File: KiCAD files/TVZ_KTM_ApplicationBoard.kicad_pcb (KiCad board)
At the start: 2 copper layers, 70 x 55 mm, 3 parts, among them J1 Conn_02x19_Odd_Even, J2 Conn_02x19_Odd_Even, U2 MCP2551-I-P

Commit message: update
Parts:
- added J3: Conn_02x19_Odd_Even, Connector_PinSocket_2.54mm:PinSocket_2x19_P2.54mm_Vertical_SMD, B.Cu at (180.5, 79.1)
- added J4: Conn_02x19_Odd_Even, Connector_PinSocket_2.54mm:PinSocket_2x19_P2.54mm_Vertical_SMD, B.Cu at (241.5, 79.1)
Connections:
- J1 pad 16: unconnected-(J1-Pad16) -> +3V3
- J1 pad 19: unconnected-(J1-Pad19) -> GND
- J1 pad 20: unconnected-(J1-Pad20) -> GND
- J1 pad 22: unconnected-(J1-Pad22) -> GND
- J1 pad 8: unconnected-(J1-Pad8) -> GND
- J2 pad 20: unconnected-(J2-Pad20) -> GND
- J2 pad 9: unconnected-(J2-Pad9) -> GND
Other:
- board size 70 x 55 mm -> 146 x 55 mm

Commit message: update
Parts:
- added C1: 100n X7R, Capacitor_SMD:C_0603_1608Metric, F.Cu at (116.4, 101.5)
- added C2: 100n X7R, Capacitor_SMD:C_0603_1608Metric, F.Cu at (215.0, 93.5)
- added C3: 100n X7R, Capacitor_SMD:C_0603_1608Metric, F.Cu at (219.0, 91.0)
- added C4: 100n X7R, Capacitor_SMD:C_0603_1608Metric, F.Cu at (215.0, 91.0)
- added D1: BLUE, LED_THT:LED_D5.0mm, F.Cu at (199.0, 62.0)
- added D10: RED, LED_THT:LED_D5.0mm, F.Cu at (130.0, 70.0)
- added D11: RED, LED_THT:LED_D5.0mm, F.Cu at (137.0, 70.0)
- added D12: RED, LED_THT:LED_D5.0mm, F.Cu at (144.0, 70.0)
- added D2: BLUE, LED_THT:LED_D5.0mm, F.Cu at (206.0, 62.0)
- added D3: BLUE, LED_THT:LED_D5.0mm, F.Cu at (213.0, 62.0)
- added D4: BLUE, LED_THT:LED_D5.0mm, F.Cu at (220.0, 62.0)
- added D5: GREEN, LED_THT:LED_D5.0mm, F.Cu at (123.0, 62.0)
- added D6: GREEN, LED_THT:LED_D5.0mm, F.Cu at (130.0, 62.0)
- added D7: GREEN, LED_THT:LED_D5.0mm, F.Cu at (137.0, 62.0)
- added D8: GREEN, LED_THT:LED_D5.0mm, F.Cu at (144.0, 62.0)
- added D9: RED, LED_THT:LED_D5.0mm, F.Cu at (123.0, 70.0)
- added JP1: Jumper_3_Open, Connector_PinHeader_2.54mm:PinHeader_1x03_P2.54mm_Vertical, F.Cu at (116.6, 88.9)
- added JP2: Jumper_2_Open, Connector_PinHeader_2.54mm:PinHeader_1x02_P2.54mm_Vertical, F.Cu at (137.4, 77.8)
- added JP3: Jumper_2_Open, Connector_PinHeader_2.54mm:PinHeader_1x02_P2.54mm_Vertical, F.Cu at (129.7, 87.5)
- added JP4: Jumper_3_Open, Connector_PinHeader_2.54mm:PinHeader_1x03_P2.54mm_Vertical, F.Cu at (132.7, 77.8)
- added JP5: Jumper_3_Open, Connector_PinHeader_2.54mm:PinHeader_1x03_P2.54mm_Vertical, F.Cu at (128.1, 77.8)
- added R1: 4k7, Resistor_SMD:R_0603_1608Metric, F.Cu at (124.9, 94.3)
- added R10: 220, Resistor_SMD:R_0603_1608Metric, F.Cu at (141.7, 76.8)
- added R11: 220, Resistor_SMD:R_0603_1608Metric, F.Cu at (149.7, 76.8)
- added R12: 220, Resistor_SMD:R_0603_1608Metric, F.Cu at (138.0, 86.5)
- added R13: 220, Resistor_SMD:R_0603_1608Metric, F.Cu at (145.7, 76.8)
- added R14: 220, Resistor_SMD:R_0603_1608Metric, F.Cu at (134.0, 91.5)
- added R15: 220, Resistor_SMD:R_0603_1608Metric, F.Cu at (129.3, 93.7)
- added R16: 220, Resistor_SMD:R_0603_1608Metric, F.Cu at (134.0, 89.0)
- added R17: 220, Resistor_SMD:R_0603_1608Metric, F.Cu at (145.7, 81.8)
- added R18: 220, Resistor_SMD:R_0603_1608Metric, F.Cu at (133.3, 94.0)
- added R19: 220, Resistor_SMD:R_0603_1608Metric, F.Cu at (138.0, 89.0)
- added R2: 4k7, Resistor_SMD:R_0603_1608Metric, F.Cu at (145.7, 79.3)
- added R3: 10k, Resistor_SMD:R_0603_1608Metric, F.Cu at (141.7, 81.8)
- added R4: 10k, Resistor_SMD:R_0603_1608Metric, F.Cu at (120.9, 94.3)
- added R5: 10k, Resistor_SMD:R_0603_1608Metric, F.Cu at (149.7, 79.3)
- added R6: 220, Resistor_SMD:R_0603_1608Metric, F.Cu at (142.0, 84.3)
- added R7: 220, Resistor_SMD:R_0603_1608Metric, F.Cu at (141.7, 79.3)
- added R8: 220, Resistor_SMD:R_0603_1608Metric, F.Cu at (134.0, 86.5)
- added R9: 220, Resistor_SMD:R_0603_1608Metric, F.Cu at (137.1, 84.0)
- added RV1: 10k, Footprints:Potentiometer_Bourns_3386P_Vertical, F.Cu at (119.8, 83.6)
- added SW1: OS102011MS2QN1, Footprints:OS102011MS2QN1, F.Cu at (198.0, 75.0)
- added SW2: OS102011MS2QN1, Footprints:OS102011MS2QN1, F.Cu at (214.0, 75.0)
- added SW3: OS102011MS2QN1, Footprints:OS102011MS2QN1, F.Cu at (206.0, 74.9)
- added SW4: OS102011MS2QN1, Footprints:OS102011MS2QN1, F.Cu at (222.0, 75.0)
- added U1: LM75B, Package_SO:SO-8_3.9x4.9mm_P1.27mm, F.Cu at (123.1, 89.8)
- added U3: MCP2551-I-P, Package_DIP:DIP-8_W7.62mm, F.Cu at (201.8, 89.0)
- moved U2 24.8 mm to (146.0, 92.0)
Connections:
- J1 pad 34: unconnected-(J1-Pad34) -> PB0_1
- J2 pad 1: unconnected-(J2-Pad1) -> PC9_1
- J2 pad 15: unconnected-(J2-Pad15) -> PA7_BUSY
- J2 pad 19: unconnected-(J2-Pad19) -> PC7_1
- J2 pad 2: unconnected-(J2-Pad2) -> PC8_1
- J2 pad 22: unconnected-(J2-Pad22) -> PB2_1
- J2 pad 23: unconnected-(J2-Pad23) -> PA8_STROBE
- J2 pad 24: unconnected-(J2-Pad24) -> PB1_1
- J2 pad 25: unconnected-(J2-Pad25) -> PB10_1
- J2 pad 4: unconnected-(J2-Pad4) -> PC6_1
- J4 pad 1: unconnected-(J4-Pad1) -> PC9_2
- J4 pad 15: unconnected-(J4-Pad15) -> PA7_BUSY
- J4 pad 19: unconnected-(J4-Pad19) -> PC7_2
- J4 pad 2: unconnected-(J4-Pad2) -> PC8_2
- J4 pad 23: unconnected-(J4-Pad23) -> PA8_STROBE
- J4 pad 4: unconnected-(J4-Pad4) -> PC6_2
- U2 pad 1: unconnected-(U2-Pad1) -> TXD_1
- U2 pad 4: unconnected-(U2-Pad4) -> RXD_1
- U2 pad 6: unconnected-(U2-Pad6) -> Net-(R18-Pad2)
- U2 pad 7: unconnected-(U2-Pad7) -> Net-(R18-Pad1)
- U2 pad 8: unconnected-(U2-Pad8) -> GND

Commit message: Update TVZ_KTM_ApplicationBoard.kicad_pcb
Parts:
- moved R10 32.6 mm to (110.6, 67.0), turned to 90 degrees
- moved D10 16.5 mm to (145.3, 63.9), turned to 90 degrees
- moved D11 16.5 mm to (152.3, 63.9), turned to 90 degrees
- moved D12 16.5 mm to (159.3, 63.9), turned to 90 degrees
- moved D9 16.5 mm to (138.3, 63.9), turned to 90 degrees
- moved D5 12.5 mm to (110.6, 63.9), turned to 90 degrees
- moved D6 12.5 mm to (117.6, 63.9), turned to 90 degrees
- moved D7 12.5 mm to (124.6, 63.9), turned to 90 degrees
- moved D8 12.5 mm to (131.6, 63.9), turned to 90 degrees

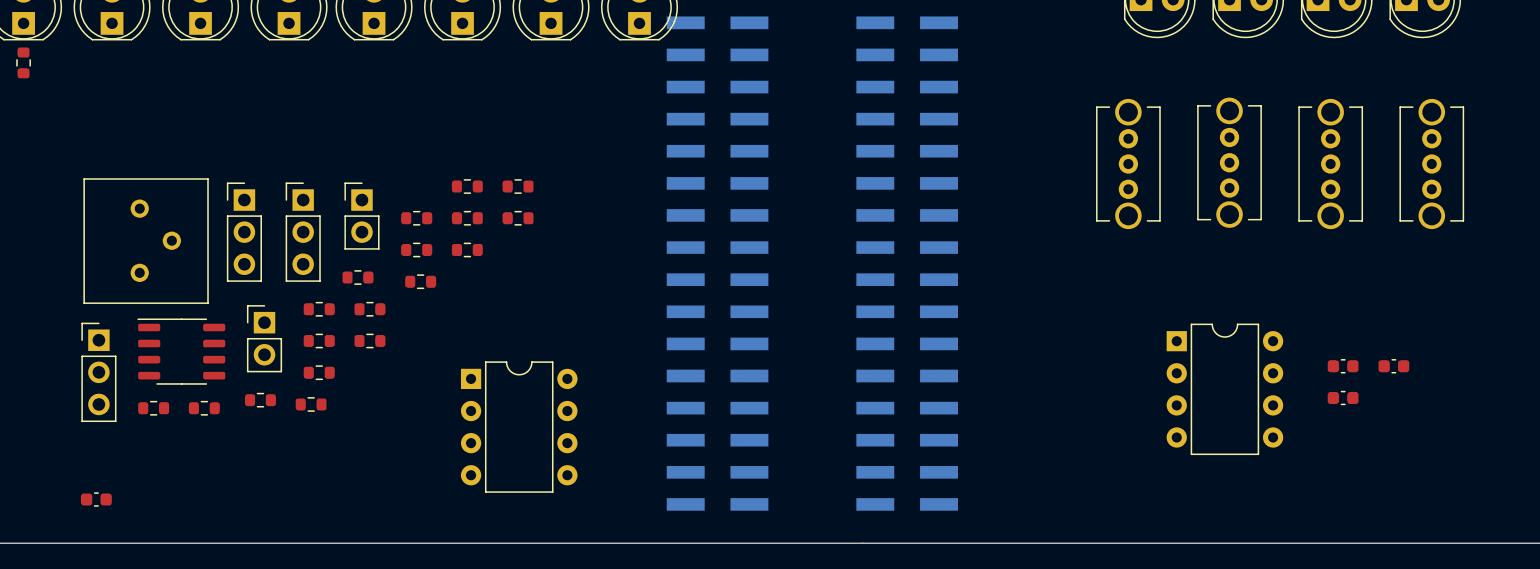
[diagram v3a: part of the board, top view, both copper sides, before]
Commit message: Update TVZ_KTM_ApplicationBoard.kicad_pcb
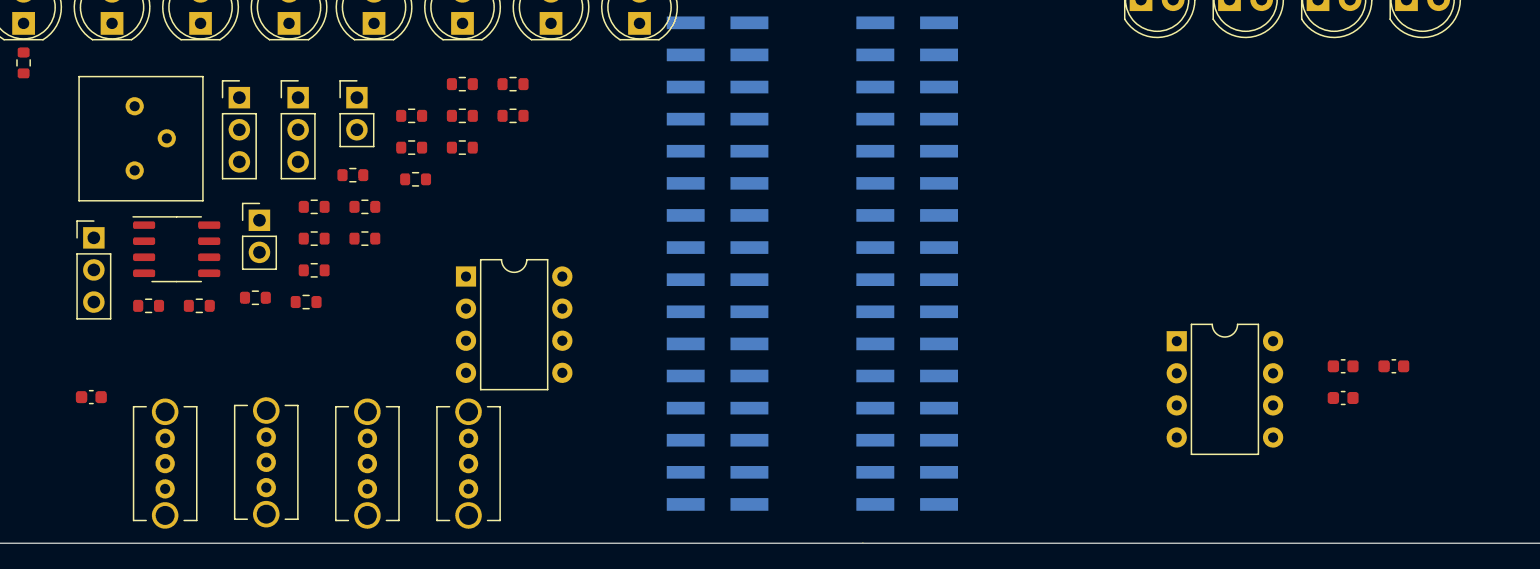
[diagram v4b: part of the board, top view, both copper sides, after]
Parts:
- moved SW1 79.8 mm to (121.8, 98.7)
- moved SW2 79.8 mm to (137.8, 98.7)
- moved SW3 79.8 mm to (129.8, 98.6)
- moved SW4 79.8 mm to (145.8, 98.7)
- moved C1 8.11 mm to (116.0, 93.4)
- moved R14 8.11 mm to (133.6, 83.4)
- moved R15 8.11 mm to (128.9, 85.6)
- moved R2 8.11 mm to (145.3, 71.2)
- moved R5 8.11 mm to (149.3, 71.2)
- moved R6 8.11 mm to (141.6, 76.2)
- moved R7 8.11 mm to (141.3, 71.2)
- moved R9 8.11 mm to (136.7, 75.9)
- moved U1 8.11 mm to (122.7, 81.7)
- moved JP1 8.11 mm to (116.2, 80.8)
- moved JP2 8.11 mm to (137.0, 69.8)
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
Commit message: update
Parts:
- D1, D10, D11, D12, D2, D3, D4, D5, D6, D7, D8, D9: footprint LED_THT:LED_D5.0mm -> LED_SMD:LED_1206_3216Metric

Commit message: update
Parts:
- removed C4: 100n X7R, Capacitor_SMD:C_0603_1608Metric
- removed RV1: 10k, Footprints:Potentiometer_Bourns_3386P_Vertical
- added D13: boja, LED_SMD:LED_1206_3216Metric, F.Cu at (229.1, 86.0)
- added JP6: Jumper_2_Open, Connector_PinHeader_2.54mm:PinHeader_1x02_P2.54mm_Vertical, F.Cu at (170.6, 66.9)
- added JP7: Jumper_2_Open, Connector_PinHeader_2.54mm:PinHeader_1x02_P2.54mm_Vertical, F.Cu at (175.3, 66.9)
- added R20: 220, Resistor_SMD:R_0805_2012Metric, F.Cu at (229.0, 88.9)
- added R21: 2k2, Resistor_SMD:R_0805_2012Metric, F.Cu at (172.5, 75.1)
- added R22: 2k2, Resistor_SMD:R_0805_2012Metric, F.Cu at (175.9, 75.1)
- added TP1: TestPoint, TestPoint:TestPoint_THTPad_D3.0mm_Drill1.5mm, F.Cu at (229.4, 101.2)
- added TP2: TestPoint, TestPoint:TestPoint_THTPad_D3.0mm_Drill1.5mm, F.Cu at (221.2, 101.3)
- added kibuzzard-63CFDED0: G***, kibuzzard-63CFDED0, F.Cu at (128.3, 101.6)
- added kibuzzard-63CFDEDE: G***, kibuzzard-63CFDEDE, F.Cu at (116.3, 101.6)
- added kibuzzard-63CFDEE9: G***, kibuzzard-63CFDEE9, F.Cu at (140.3, 101.6)
- added kibuzzard-63CFDEF4: G***, kibuzzard-63CFDEF4, F.Cu at (152.3, 101.6)
- C1, C2, C3: footprint Capacitor_SMD:C_0603_1608Metric -> Capacitor_SMD:C_0805_2012Metric
- R1, R2: value 4k7 -> 10k; footprint Resistor_SMD:R_0603_1608Metric -> Resistor_SMD:R_0805_2012Metric
- R10, R11, R12, R13, R14, R15, R16, R17, R18, R19, R3, R4, R5, R6, R7, R8, R9: footprint Resistor_SMD:R_0603_1608Metric -> Resistor_SMD:R_0805_2012Metric
- SW1, SW2, SW3, SW4: value OS102011MS2QN1 -> EG1271A; footprint Footprints:OS102011MS2QN1 -> Footprint:EG1271A
- moved C2 92.3 mm to (127.5, 64.2), turned to 90 degrees
- moved R9 84.2 mm to (220.6, 82.0)
- moved R8 80.2 mm to (213.7, 80.5)
- moved JP1 72.8 mm to (187.8, 93.6)
- moved JP5 71.9 mm to (195.5, 93.6)
- moved R19 70.0 mm to (205.7, 64.9), turned to 90 degrees
- moved R7 66.3 mm to (206.9, 81.0)
- moved JP4 63.9 mm to (191.6, 93.6)
- moved R4 59.2 mm to (178.6, 97.9)
- moved C1 58.9 mm to (174.9, 93.9), turned to 90 degrees
- moved R6 58.2 mm to (199.6, 81.2)
- moved U1 49.1 mm to (169.4, 96.8)
- moved R3 43.4 mm to (178.6, 95.9)
- moved R5 40.9 mm to (178.6, 99.8)
- moved R1 30.6 mm to (155.1, 84.8), turned to 90 degrees
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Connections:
- C2 pad 1: +3V3 -> +5V
- C3 pad 1: +3V3 -> +5V
- J1 pad 18: unconnected-(J1-Pad18) -> +5V
- J1 pad 21: unconnected-(J1-Pad21) -> PB7_1
- J1 pad 32: unconnected-(J1-Pad32) -> PA4_1
- J2 pad 12: unconnected-(J2-Pad12) -> PA12_1
- J2 pad 14: unconnected-(J2-Pad14) -> PA11_1
- J2 pad 16: unconnected-(J2-Pad16) -> PB12_1
- J2 pad 17: unconnected-(J2-Pad17) -> PB6_~{CS}
- J2 pad 21: unconnected-(J2-Pad21) -> PA9_1
- J2 pad 26: unconnected-(J2-Pad26) -> PB15_1
- J2 pad 27: unconnected-(J2-Pad27) -> PB4_MISO
- J2 pad 28: unconnected-(J2-Pad28) -> PB14_1
- J2 pad 29: unconnected-(J2-Pad29) -> PB5_MOSI
- J2 pad 30: unconnected-(J2-Pad30) -> PB13_1
- J2 pad 31: unconnected-(J2-Pad31) -> PB3_SCK
- J2 pad 33: unconnected-(J2-Pad33) -> PA10_1
- J3 pad 21: unconnected-(J3-Pad21) -> PB7_1
- J3 pad 32: unconnected-(J3-Pad32) -> PA4_2
- J4 pad 12: unconnected-(J4-Pad12) -> PA12_2
- J4 pad 13: unconnected-(J4-Pad13) -> PA4_1
- J4 pad 14: unconnected-(J4-Pad14) -> PA11_2
- J4 pad 16: unconnected-(J4-Pad16) -> PB12_1
- J4 pad 17: unconnected-(J4-Pad17) -> PB6_~{CS}
- J4 pad 21: unconnected-(J4-Pad21) -> PA10_1
- J4 pad 26: unconnected-(J4-Pad26) -> PB15_1
- J4 pad 27: unconnected-(J4-Pad27) -> PB4_MISO
- J4 pad 28: unconnected-(J4-Pad28) -> PB14_1
- J4 pad 29: unconnected-(J4-Pad29) -> PB5_MOSI
- J4 pad 30: unconnected-(J4-Pad30) -> PB13_1
- J4 pad 31: unconnected-(J4-Pad31) -> PB3_SCK
- J4 pad 33: unconnected-(J4-Pad33) -> PA9_1
- JP2 pad 1: Net-(JP2-Pad1) -> +3V3
- JP2 pad 2: /SCL -> Net-(JP2-Pad2)
- JP3 pad 1: Net-(JP3-Pad1) -> +3V3
- JP3 pad 2: /SDA -> Net-(JP3-Pad2)
- R1 pad 1: Net-(JP2-Pad1) -> PB6_~{CS}
- R1 pad 2: +3V3 -> Net-(JP2-Pad2)
- R2 pad 1: Net-(JP3-Pad1) -> PB7_1
- R2 pad 2: +3V3 -> Net-(JP3-Pad2)
- SW2 pad 2: PB2_1 -> PB1_1
- SW3 pad 2: PB1_1 -> PB2_1
- U1 pad 1: /SDA -> PB7_1
- U1 pad 2: /SCL -> PB6_~{CS}
- U2 pad 1: TXD_1 -> PA12_1
- U2 pad 3: +3V3 -> +5V
- U2 pad 4: RXD_1 -> PA11_1
- U3 pad 1: TXD_2 -> PA12_2
- U3 pad 3: +3V3 -> +5V
- U3 pad 4: RXD_2 -> PA11_2

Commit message: update
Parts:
- removed kibuzzard-63CFDED0: G***, kibuzzard-63CFDED0
- removed kibuzzard-63CFDEDE: G***, kibuzzard-63CFDEDE
- removed kibuzzard-63CFDEE9: G***, kibuzzard-63CFDEE9
- removed kibuzzard-63CFDEF4: G***, kibuzzard-63CFDEF4
- added TP10: TestPoint, Footprint:KEYS4952, F.Cu at (189.0, 125.0)
- added TP11: TestPoint, Footprint:KEYS4952, F.Cu at (179.0, 125.0)
- added TP12: TestPoint, Footprint:KEYS4952, F.Cu at (119.1, 125.0)
- added TP13: TestPoint, Footprint:KEYS4952, F.Cu at (112.0, 125.0)
- added TP14: TestPoint, Footprint:KEYS4952, F.Cu at (182.0, 135.0)
- added TP3: TestPoint, Footprint:KEYS4952, F.Cu at (170.0, 112.0)
- added TP4: TestPoint, Footprint:KEYS4952, F.Cu at (182.0, 112.0)
- added TP5: TestPoint, Footprint:KEYS4952, F.Cu at (113.0, 101.5)
- added TP6: TestPoint, Footprint:KEYS4952, F.Cu at (124.0, 101.5)
- added TP7: TestPoint, Footprint:KEYS4952, F.Cu at (146.0, 101.5)
- added TP8: TestPoint, Footprint:KEYS4952, F.Cu at (135.0, 101.5)
- added TP9: TestPoint, Footprint:KEYS4952, F.Cu at (173.0, 101.4)
- added kibuzzard-63D0F0B6: G***, kibuzzard-63D0F0B6, F.Cu at (235.0, 54.0)
- added kibuzzard-63D0F0B6: G***, kibuzzard-63D0F0B6, F.Cu at (159.0, 54.0)
- added kibuzzard-63D0FB98: G***, kibuzzard-63D0FB98, F.Cu at (124.0, 98.0)
- added kibuzzard-63D0FBA8: G***, kibuzzard-63D0FBA8, F.Cu at (113.0, 98.0)
- added kibuzzard-63D0FBB4: G***, kibuzzard-63D0FBB4, F.Cu at (146.0, 98.0)
- added kibuzzard-63D0FBBC: G***, kibuzzard-63D0FBBC, F.Cu at (135.0, 98.0)
- added kibuzzard-63D0FBC8: G***, kibuzzard-63D0FBC8, F.Cu at (173.0, 87.9)
- added kibuzzard-63D0FC24: G***, kibuzzard-63D0FC24, F.Cu at (116.0, 82.6)
- added kibuzzard-63D0FC34: G***, kibuzzard-63D0FC34, F.Cu at (128.5, 82.6)
- added kibuzzard-63D0FC3F: G***, kibuzzard-63D0FC3F, F.Cu at (140.0, 82.6)
- added kibuzzard-63D0FC48: G***, kibuzzard-63D0FC48, F.Cu at (152.0, 82.6)
- added kibuzzard-63D0FCA0: G***, kibuzzard-63D0FCA0, F.Cu at (170.0, 116.0)
- added kibuzzard-63D0FCA9: G***, kibuzzard-63D0FCA9, F.Cu at (182.0, 116.0)
- added kibuzzard-63D121CA: G***, kibuzzard-63D121CA, F.Cu at (189.0, 129.0)
- added kibuzzard-63D12226: G***, kibuzzard-63D12226, F.Cu at (112.1, 129.0)
- added kibuzzard-63D12234: G***, kibuzzard-63D12234, F.Cu at (119.1, 129.0)
- added kibuzzard-63D1223E: G***, kibuzzard-63D1223E, F.Cu at (179.0, 129.0)
- added kibuzzard-63D123B4: G***, kibuzzard-63D123B4, F.Cu at (182.0, 139.0)
- added kibuzzard-63D12AAF: G***, kibuzzard-63D12AAF, F.Cu at (113.0, 93.4)
- added kibuzzard-63D12AD6: G***, kibuzzard-63D12AD6, F.Cu at (119.0, 93.4)
- added kibuzzard-63D12AE3: G***, kibuzzard-63D12AE3, F.Cu at (125.5, 93.4)
- added kibuzzard-63D12AEC: G***, kibuzzard-63D12AEC, F.Cu at (157.0, 93.4)
- added kibuzzard-63D12AEC: G***, kibuzzard-63D12AEC, F.Cu at (139.0, 93.4)
- added kibuzzard-63D12AEC: G***, kibuzzard-63D12AEC, F.Cu at (131.5, 93.4)
- added kibuzzard-63D12AEC: G***, kibuzzard-63D12AEC, F.Cu at (145.0, 93.4)
- added kibuzzard-63D12AEC: G***, kibuzzard-63D12AEC, F.Cu at (151.0, 93.4)
- added kibuzzard-63D12B8B: G***, kibuzzard-63D12B8B, F.Cu at (108.5, 90.4)
- added kibuzzard-63D13186: G***, kibuzzard-63D13186, F.Cu at (157.0, 98.0)
- TP1, TP2: footprint TestPoint:TestPoint_THTPad_D3.0mm_Drill1.5mm -> Footprint:KEYS4952
- moved R5 92.1 mm to (179.8, 7.77), turned to 90 degrees
- moved R4 90.1 mm to (177.8, 7.77), turned to 90 degrees
- moved R3 88.2 mm to (175.7, 7.77), turned to 90 degrees
- moved C1 82.4 mm to (171.0, 11.6), turned to 180 degrees
- moved U1 79.9 mm to (173.9, 17.0), turned to 90 degrees
- moved TP2 64.2 mm to (157.0, 101.5)
- moved R1 63.4 mm to (175.7, 24.9), turned to -90 degrees
- moved R2 61.4 mm to (172.0, 24.9), turned to -90 degrees
- moved TP1 57.2 mm to (173.0, 91.4)
- moved JP2 48.4 mm to (174.6, 32.8), turned to 180 degrees
- moved JP3 46.0 mm to (171.6, 32.8), turned to 180 degrees
- moved JP1 32.6 mm to (188.0, 61.0)
- moved JP4 32.6 mm to (191.8, 61.0)
- moved JP5 32.6 mm to (195.6, 61.0)
- moved R22 29.4 mm to (171.6, 46.0)
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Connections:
- net Net-(R18-Pad1) renamed /CANH
- net Net-(R18-Pad2) renamed /CANL

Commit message: update
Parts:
- added kibuzzard-63D17008: G***, kibuzzard-63D17008, F.Cu at (108.5, 100.0)
- added kibuzzard-63D171DF: G***, kibuzzard-63D171DF, F.Cu at (131.1, 100.1)
- moved SW1 1.01 mm to (116.0, 76.5)
- moved SW2 1.01 mm to (140.4, 76.5)
- moved SW3 1.01 mm to (128.4, 76.5)
- moved SW4 1.01 mm to (152.4, 76.5)
- moved kibuzzard-63D0FC3F 0.54 mm to (140.4, 83.0)
- moved kibuzzard-63D0FC48 0.54 mm to (152.4, 83.0)
- moved kibuzzard-63D0FC34 0.41 mm to (128.4, 83.0)
- moved kibuzzard-63D0FC24 0.39 mm to (116.0, 83.0)
